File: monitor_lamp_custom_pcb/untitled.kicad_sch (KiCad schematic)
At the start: 9 parts, among them J2 VEML7700_Connection, J3 LD2410C_Connection, J4 Conn_01x02, Q2 IRLZ44N, U3 ESP32-C3_SUPERMINI_TH, U4 MAX40200AUK

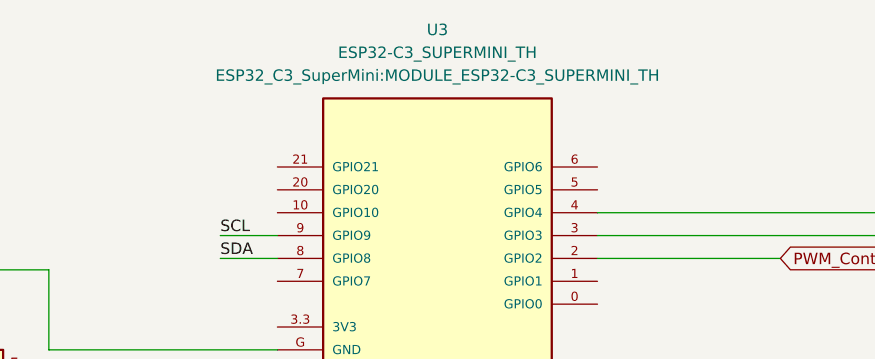
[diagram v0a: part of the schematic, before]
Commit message: Added custom library component to the project
In Kicad not all components are present in the default library, some sensors or modules have to be manually added importing symbols and footprint.
Putting this components inside the project is useful so if someone will download it, in is not necessary to search and import the components
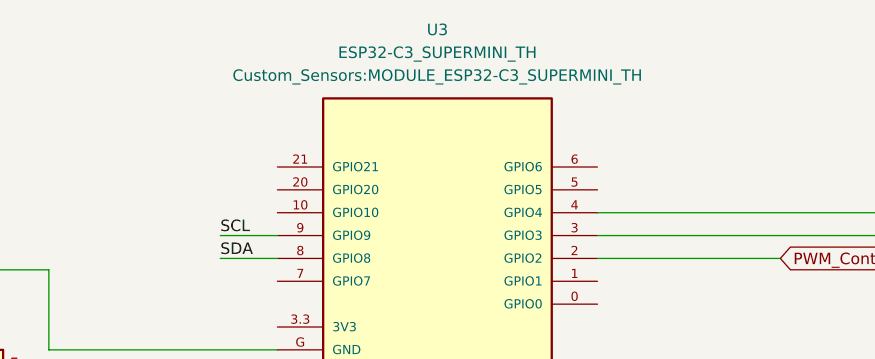
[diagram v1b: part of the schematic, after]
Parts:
- U3: footprint ESP32_C3_SuperMini:MODULE_ESP32-C3_SUPERMINI_TH -> Custom_Sensors:MODULE_ESP32-C3_SUPERMINI_TH

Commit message: Started to place component in the pcb design.
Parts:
- J4: footprint TerminalBlock_Phoenix:TerminalBlock_Phoenix_PT-1,5-2-5.0-H_1x02_P5.00mm_Horizontal -> TerminalBlock:TerminalBlock_Xinya_XY308-2.54-2P_1x02_P2.54mm_Horizontal
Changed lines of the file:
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@@
 			)
 		)
-		(property "Footprint" "TerminalBlock_Phoenix:TerminalBlock_Phoenix_PT-1,5-2-5.0-H_1x02_P5.00mm_Horizontal"
+		(property "Footprint" "TerminalBlock:TerminalBlock_Xinya_XY308-2.54-2P_1x02_P2.54mm_Horizontal"
 			(at 209.55 132.08 0)
 			(hide yes)

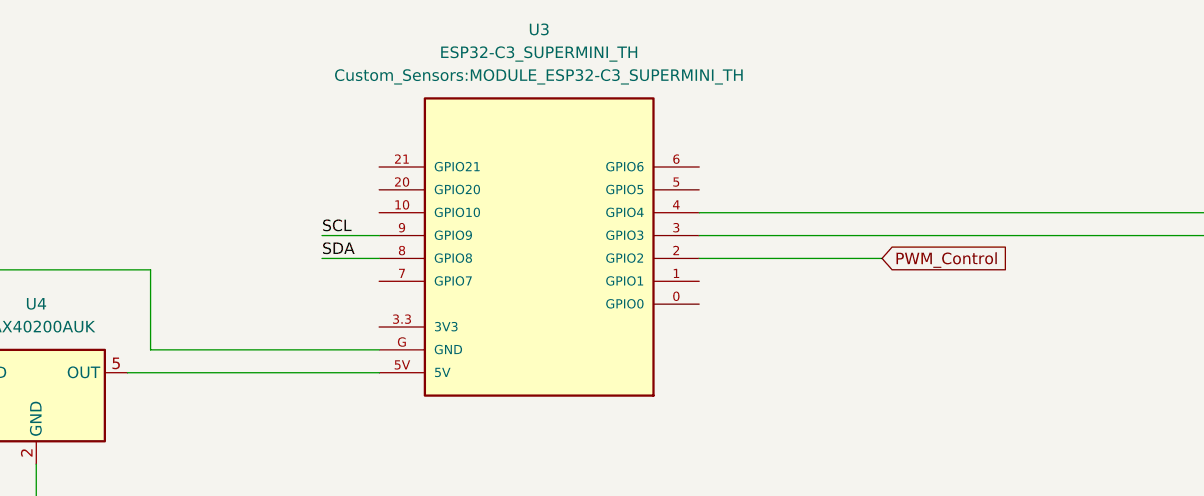
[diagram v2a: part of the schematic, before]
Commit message: Started to place components on the board layout
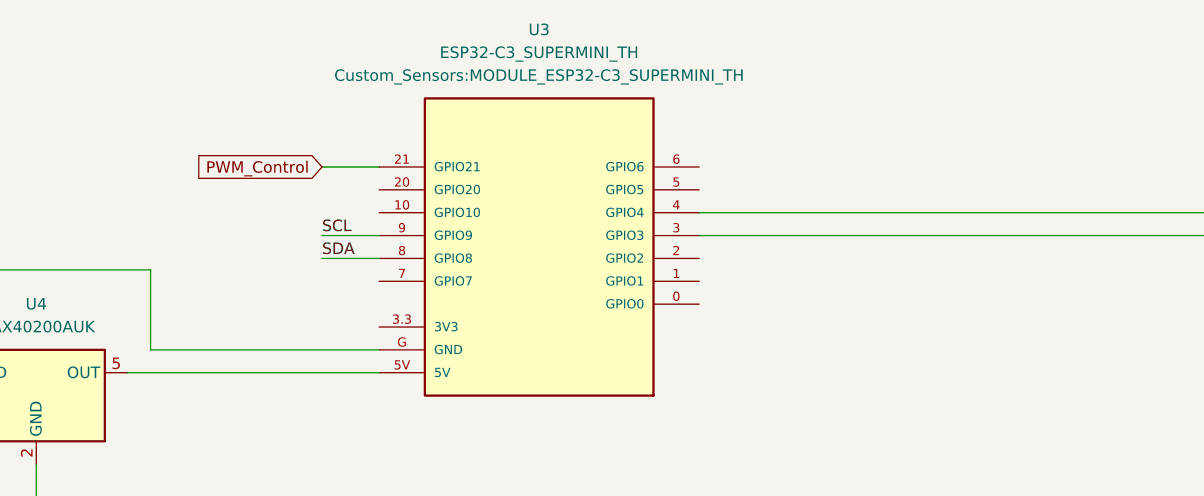
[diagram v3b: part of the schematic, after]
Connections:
- net PWM_Control: now also U3.21 (GPIO21); no longer U3.2 (GPIO2)
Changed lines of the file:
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@@
-	(wire
-		(pts
-			(xy 157.48 53.34) (xy 177.8 53.34)
-		)
-		(stroke
-			(width 0)
-			(type default)
-		)
-	)
 	(wire
 		(pts
@@
 		(pts
 			(xy 157.48 48.26) (xy 228.6 48.26)
+		)
+		(stroke
+			(width 0)
+			(type default)
+		)
+	)
+	(wire
+		(pts
+			(xy 115.57 43.18) (xy 121.92 43.18)
 		)
 		(stroke
@@
 	(global_label "PWM_Control"
 		(shape input)
-		(at 177.8 53.34 0)
+		(at 115.57 43.18 180)
 		(fields_autoplaced yes)
 		(effects
@@
 				(size 1.27 1.27)
 			)
-			(justify left)
+			(justify right)
 		)
 		(property "Intersheetrefs" "${INTERSHEET_REFS}"
-			(at 192.8197 53.34 0)
+			(at 100.5503 43.18 0)
 			(hide yes)
 			(show_name no)
@@
 					(size 1.27 1.27)
 				)
-				(justify left)
-			)
-		)
+				(justify right)
+			)
+		)

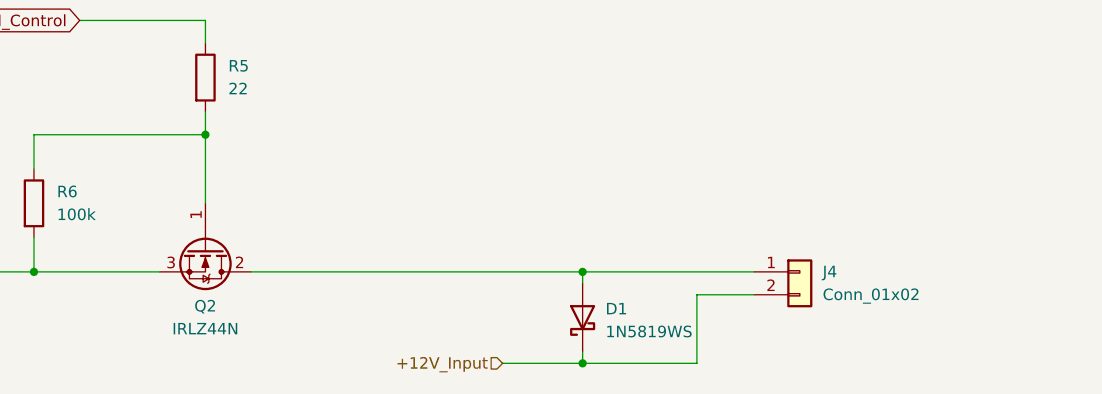
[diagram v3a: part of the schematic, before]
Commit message: Added almost all components to the board. Next step trace
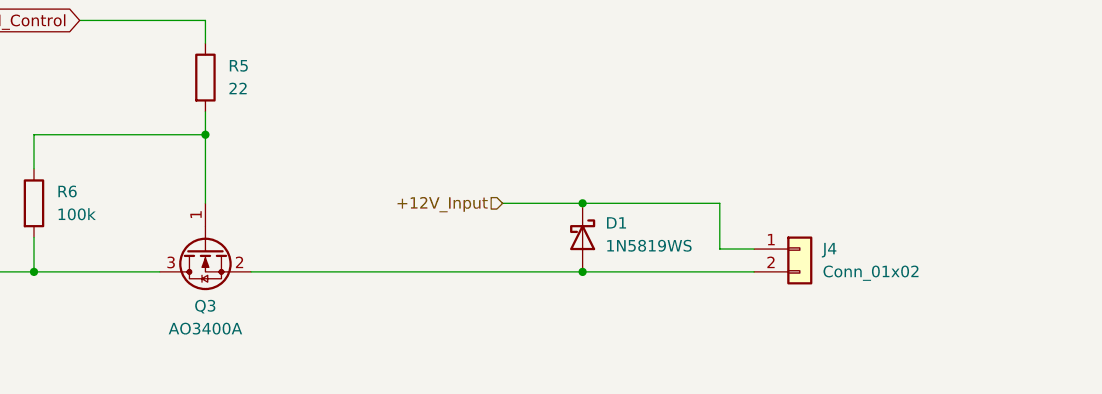
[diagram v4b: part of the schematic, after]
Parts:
- removed Q2: IRLZ44N, Package_TO_SOT_THT:TO-220-3_Vertical, symbol Transistor_FET:IRLZ44N
- added Q3: AO3400A, Package_TO_SOT_SMD:SOT-23, symbol Transistor_FET:AO3400A
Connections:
- net +12V_Input: now also J4.1 (Pin_1); no longer J4.2 (Pin_2)
- net GND: now also Q3.3 (D)
- net at R5.2, R6.1: now also Q3.1 (G)
- net at D1.2 (A): now also J4.2 (Pin_2), Q3.2 (S); no longer J4.1 (Pin_1)
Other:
- moved on the sheet: D1, J4
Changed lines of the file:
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@@
 	(paper "A4")
+	(junction
+		(at 185.42 132.08)
+		(diameter 0)
+		(color 0 0 0 0)
+	)
 	(junction
 		(at 124.46 132.08)
@@
 	)
 	(junction
-		(at 185.42 142.24)
-		(diameter 0)
-		(color 0 0 0 0)
-	)
-	(junction
-		(at 185.42 132.08)
+		(at 185.42 124.46)
 		(diameter 0)
 		(color 0 0 0 0)
@@
 	(wire
 		(pts
+			(xy 220.98 74.93) (xy 228.6 74.93)
+		)
+		(stroke
+			(width 0)
+			(type default)
+		)
+	)
+	(wire
+		(pts
+			(xy 93.98 66.04) (xy 121.92 66.04)
+		)
+		(stroke
+			(width 0)
+			(type default)
+		)
+	)
+	(wire
+		(pts
+			(xy 220.98 80.01) (xy 228.6 80.01)
+		)
+		(stroke
+			(width 0)
+			(type default)
+		)
+	)
+	(wire
+		(pts
+			(xy 176.53 124.46) (xy 185.42 124.46)
+		)
+		(stroke
+			(width 0)
+			(type default)
+		)
+	)
+	(wire
+		(pts
 			(xy 185.42 132.08) (xy 204.47 132.08)
 		)
@@
 	(wire
 		(pts
-			(xy 220.98 74.93) (xy 228.6 74.93)
-		)
-		(stroke
-			(width 0)
-			(type default)
-		)
-	)
-	(wire
-		(pts
-			(xy 93.98 66.04) (xy 121.92 66.04)
-		)
-		(stroke
-			(width 0)
-			(type default)
-		)
-	)
-	(wire
-		(pts
-			(xy 220.98 80.01) (xy 228.6 80.01)
-		)
-		(stroke
-			(width 0)
-			(type default)
-		)
-	)
-	(wire
-		(pts
-			(xy 185.42 140.97) (xy 185.42 142.24)
-		)
-		(stroke
-			(width 0)
-			(type default)
-		)
-	)
-	(wire
-		(pts
 			(xy 66.04 66.04) (xy 66.04 71.12)
 		)
@@
 	(wire
 		(pts
-			(xy 185.42 142.24) (xy 198.12 142.24)
-		)
-		(stroke
-			(width 0)
-			(type default)
-		)
-	)
-	(wire
-		(pts
 			(xy 96.52 54.61) (xy 96.52 63.5)
 		)
@@
 	(wire
 		(pts
-			(xy 185.42 132.08) (xy 185.42 133.35)
-		)
-		(stroke
-			(width 0)
-			(type default)
-		)
-	)
-	(wire
-		(pts
-			(xy 198.12 134.62) (xy 204.47 134.62)
+			(xy 204.47 129.54) (xy 200.66 129.54)
 		)
 		(stroke
@@
 	(wire
 		(pts
+			(xy 200.66 129.54) (xy 200.66 124.46)
+		)
+		(stroke
+			(width 0)
+			(type default)
+		)
+	)
+	(wire
+		(pts
+			(xy 200.66 124.46) (xy 185.42 124.46)
+		)
+		(stroke
+			(width 0)
+			(type default)
+		)
+	)
+	(wire
+		(pts
 			(xy 43.18 132.08) (xy 124.46 132.08)
-		)
-		(stroke
-			(width 0)
-			(type default)
-		)
-	)
-	(wire
-		(pts
-			(xy 198.12 142.24) (xy 198.12 134.62)
-		)
-		(stroke
-			(width 0)
-			(type default)
-		)
-	)
-	(wire
-		(pts
-			(xy 176.53 142.24) (xy 185.42 142.24)
 		)
 		(stroke
@@
 	(hierarchical_label "+12V_Input"
 		(shape input)
-		(at 176.53 142.24 180)
+		(at 176.53 124.46 180)
 		(effects
 			(font
@@
 	)
 	(symbol
-		(lib_id "Transistor_FET:IRLZ44N")
-		(at 143.51 129.54 270)
-		(unit 1)
-		(body_style 1)
-		(exclude_from_sim no)
-		(in_bom yes)
-		(on_board yes)
-		(in_pos_files yes)
-		(dnp no)
-		(fields_autoplaced yes)
-		(property "Reference" "Q2"
-			(at 143.51 135.89 90)
-			(show_name no)
-			(do_not_autoplace no)
-			(effects
-				(font
-					(size 1.27 1.27)
-				)
-			)
-		)
-		(property "Value" "IRLZ44N"
-			(at 143.51 138.43 90)
-			(show_name no)
-			(do_not_autoplace no)
-			(effects
-				(font
-					(size 1.27 1.27)
-				)
-			)
-		)
-		(property "Footprint" "Package_TO_SOT_THT:TO-220-3_Vertical"
-			(at 141.605 134.62 0)
-			(hide yes)
-			(show_name no)
-			(do_not_autoplace no)
-			(effects
-				(font
-					(size 1.27 1.27)
-					(italic yes)
-				)
-				(justify left)
-			)
-		)
-		(property "Datasheet" "http://www.irf.com/product-info/datasheets/data/irlz44n.pdf"
-			(at 139.7 134.62 0)
-			(hide yes)
-			(show_name no)
-			(do_not_autoplace no)
-			(effects
-				(font
-					(size 1.27 1.27)
-				)
-				(justify left)
-			)
-		)
-		(property "Description" "47A Id, 55V Vds, 22mOhm Rds Single N-Channel HEXFET Power MOSFET, TO-220AB"
-			(at 143.51 129.54 0)
-			(hide yes)
-			(show_name no)
-			(do_not_autoplace no)
-			(effects
-				(font
-					(size 1.27 1.27)
-				)
-			)
-		)
-		(pin "2"
-		)
-		(pin "1"
-		)
-		(pin "3"
-		)
-		(instances
-			(project "monitor_lamp_custom_pcb"
-				(path "/77ed2f8f-6c9e-49d8-b473-d071fcc9ba2f/0d662d48-a846-4d52-8851-1394daa2469c"
-					(reference "Q2")
-					(unit 1)
-				)
-			)
-		)
-	)
-	(symbol
 		(lib_id "power:GND")
 		(at 220.98 86.36 0)
@@
 	)
 	(symbol
+		(lib_id "Transistor_FET:AO3400A")
+		(at 143.51 129.54 90)
+		(mirror x)
+		(unit 1)
+		(body_style 1)
+		(exclude_from_sim no)
+		(in_bom yes)
+		(on_board yes)
+		(in_pos_files yes)
+		(dnp no)
+		(property "Reference" "Q3"
+			(at 143.51 135.89 90)
+			(show_name no)
+			(do_not_autoplace no)
+			(effects
+				(font
+					(size 1.27 1.27)
+				)
+			)
+		)
+		(property "Value" "AO3400A"
+			(at 143.51 138.43 90)
+			(show_name no)
+			(do_not_autoplace no)
+			(effects
+				(font
+					(size 1.27 1.27)
+				)
+			)
+		)
+		(property "Footprint" "Package_TO_SOT_SMD:SOT-23"
+			(at 145.415 134.62 0)
+			(hide yes)
+			(show_name no)
+			(do_not_autoplace no)
+			(effects
+				(font
+					(size 1.27 1.27)
+					(italic yes)
+				)
+				(justify left)
+			)
+		)
+		(property "Datasheet" "http://www.aosmd.com/pdfs/datasheet/AO3400A.pdf"
+			(at 147.32 134.62 0)
+			(hide yes)
+			(show_name no)
+			(do_not_autoplace no)
+			(effects
+				(font
+					(size 1.27 1.27)
+				)
+				(justify left)
+			)
+		)
+		(property "Description" "30V Vds, 5.7A Id, N-Channel MOSFET, SOT-23"
+			(at 143.51 129.54 0)
+			(hide yes)
+			(show_name no)
+			(do_not_autoplace no)
+			(effects
+				(font
+					(size 1.27 1.27)
+				)
+			)
+		)
+		(pin "3"
+		)
+		(pin "2"
+		)
+		(pin "1"
+		)
+		(instances
+			(project "monitor_lamp_custom_pcb"
+				(path "/77ed2f8f-6c9e-49d8-b473-d071fcc9ba2f/0d662d48-a846-4d52-8851-1394daa2469c"
+					(reference "Q3")
+					(unit 1)
+				)
+			)
+		)
+	)
+	(symbol
 		(lib_id "Connector_Generic:Conn_01x02")
-		(at 209.55 132.08 0)
+		(at 209.55 129.54 0)
 		(unit 1)
 		(body_style 1)
@@
 		(fields_autoplaced yes)
 		(property "Reference" "J4"
+			(at 212.09 129.5399 0)
+			(show_name no)
+			(do_not_autoplace no)
+			(effects
+				(font
+					(size 1.27 1.27)
+				)
+				(justify left)
+			)
+		)
+		(property "Value" "Conn_01x02"
 			(at 212.09 132.0799 0)
 			(show_name no)
@@
 			)
 		)
-		(property "Value" "Conn_01x02"
-			(at 212.09 134.6199 0)
-			(show_name no)
-			(do_not_autoplace no)
-			(effects
-				(font
-					(size 1.27 1.27)
-				)
-				(justify left)
-			)
-		)
 		(property "Footprint" "TerminalBlock:TerminalBlock_Xinya_XY308-2.54-2P_1x02_P2.54mm_Horizontal"
-			(at 209.55 132.08 0)
+			(at 209.55 129.54 0)
 			(hide yes)
 			(show_name no)
@@
 		)
 		(property "Datasheet" ""
-			(at 209.55 132.08 0)
+			(at 209.55 129.54 0)
 			(hide yes)
 			(show_name no)
@@
 		)
 		(property "Description" "Generic connector, single row, 01x02, script generated (kicad-library-utils/schlib/autogen/connector/)"
-			(at 209.55 132.08 0)
+			(at 209.55 129.54 0)
 			(hide yes)
 			(show_name no)
@@
 	(symbol
 		(lib_id "Diode:1N5819WS")
-		(at 185.42 137.16 90)
+		(at 185.42 128.27 270)
 		(unit 1)
 		(body_style 1)
@@
 		(fields_autoplaced yes)
 		(property "Reference" "D1"
-			(at 187.96 136.2074 90)
-			(show_name no)
-			(do_not_autoplace no)
-			(effects
-				(font
-					(size 1.27 1.27)
-				)
-				(justify right)
+			(at 187.96 126.6824 90)
+			(show_name no)
+			(do_not_autoplace no)
+			(effects
+				(font
+					(size 1.27 1.27)
+				)
+				(justify left)
 			)
 		)
 		(property "Value" "1N5819WS"
-			(at 187.96 138.7474 90)
-			(show_name no)
-			(do_not_autoplace no)
-			(effects
-				(font
-					(size 1.27 1.27)
-				)
-				(justify right)
+			(at 187.96 129.2224 90)
+			(show_name no)
+			(do_not_autoplace no)
+			(effects
+				(font
+					(size 1.27 1.27)
+				)
+				(justify left)
 			)
 		)
 		(property "Footprint" "Diode_SMD:D_SOD-323"
-			(at 189.865 137.16 0)
+			(at 180.975 128.27 0)
 			(hide yes)
 			(show_name no)
@@
 		)
 		(property "Datasheet" "https://datasheet.lcsc.com/lcsc/2204281430_Guangdong-Hottech-1N5819WS_C191023.pdf"
-			(at 185.42 137.16 0)
+			(at 185.42 128.27 0)
 			(hide yes)
 			(show_name no)
@@
 		)
 		(property "Description" "40V 600mV@1A 1A SOD-323 Schottky Barrier Diodes, SOD-323"
-			(at 185.42 137.16 0)
-			(hide yes)
-			(show_name no)
+			(at 185.42 128.27 0)
+			(hide yes)
+			(show_name no)

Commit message: Placed all components, changed the J2 & J3 connectors
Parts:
- J2, J3: footprint Connector_PinHeader_2.54mm:PinHeader_1x04_P2.54mm_Horizontal -> Connector_JST:JST_SH_BM04B-SRSS-TB_1x04-1MP_P1.00mm_Vertical
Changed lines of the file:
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@@
 			)
 		)
-		(property "Footprint" "Connector_PinHeader_2.54mm:PinHeader_1x04_P2.54mm_Horizontal"
+		(property "Footprint" "Connector_JST:JST_SH_BM04B-SRSS-TB_1x04-1MP_P1.00mm_Vertical"
 			(at 233.68 77.47 0)
 			(hide yes)
@@
 			)
 		)
-		(property "Footprint" "Connector_PinHeader_2.54mm:PinHeader_1x04_P2.54mm_Horizontal"
+		(property "Footprint" "Connector_JST:JST_SH_BM04B-SRSS-TB_1x04-1MP_P1.00mm_Vertical"
 			(at 233.68 48.26 0)
 			(hide yes)

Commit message: Tracing some routes
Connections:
- net +5V is gone; now on net 5V_Protected: J2.1 (Pin_1), J3.1 (Pin_1)
- net 5V_Protected: now reaches U3.5V, U4.5 (OUT)
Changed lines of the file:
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@@
 	(wire
 		(pts
-			(xy 220.98 45.72) (xy 228.6 45.72)
+			(xy 215.9 45.72) (xy 228.6 45.72)
 		)
 		(stroke
@@
 	(wire
 		(pts
-			(xy 220.98 74.93) (xy 228.6 74.93)
+			(xy 215.9 74.93) (xy 228.6 74.93)
 		)
 		(stroke
@@
 		)
 	)
-	(label "+5V"
-		(at 220.98 74.93 0)
-		(effects
-			(font
-				(size 1.27 1.27)
-			)
-			(justify left bottom)
-		)
-	)
-	(label "+5V"
-		(at 220.98 45.72 0)
-		(effects
-			(font
+	(label "5V_Protected"
+		(at 97.79 66.04 0)
+		(effects
+			(font
+				(size 1.27 1.27)
+			)
+			(justify left bottom)
+		)
+	)
+	(label "5V_Protected"
+		(at 215.9 74.93 0)
+		(effects
+			(font
+				(size 1.27 1.27)
+			)
+			(justify left bottom)
+		)
+	)
+	(label "5V_Protected"
+		(at 215.9 45.72 0)
+		(effects
+			(font

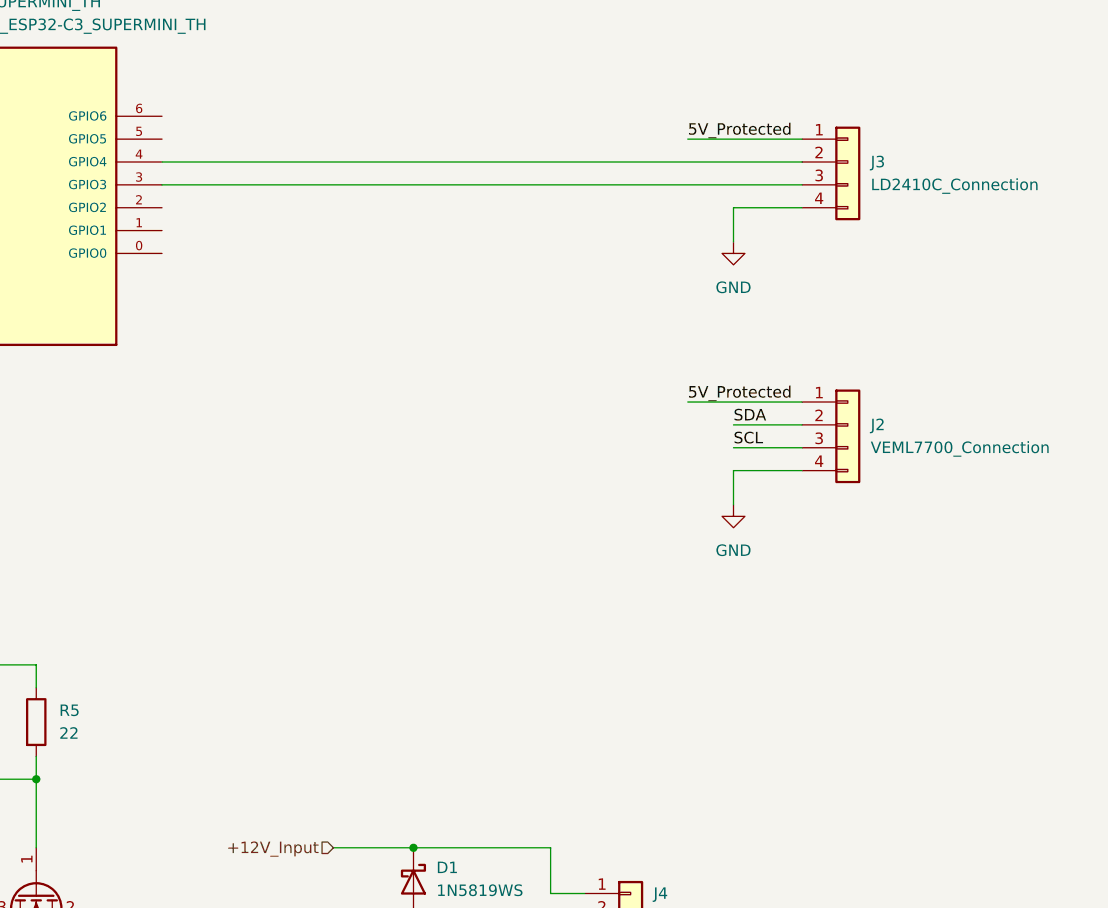
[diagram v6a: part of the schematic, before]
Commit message: Added connection for temp sensor
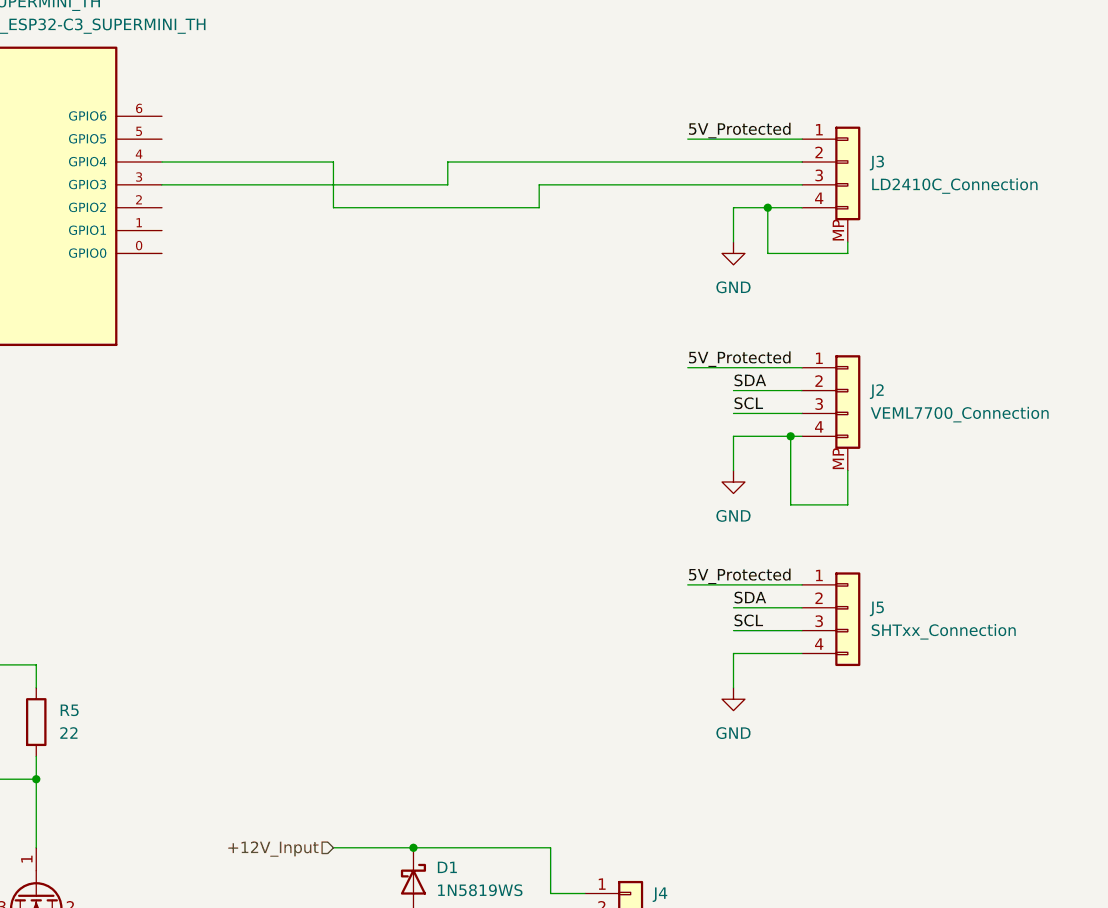
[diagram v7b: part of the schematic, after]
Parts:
- added J5: SHTxx_Connection, Connector_PinHeader_2.54mm:PinHeader_1x04_P2.54mm_Vertical, symbol Connector_Generic:Conn_01x04
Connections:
- net 5V_Protected: now also J5.1 (Pin_1)
- net GND: now also J2.MP, J3.MP, J5.4 (Pin_4)
- net SCL: now also J5.3 (Pin_3)
- net SDA: now also J5.2 (Pin_2)
- net at J3.2 (Pin_2): now also U3.3 (GPIO3); no longer U3.4 (GPIO4)
- net at J3.3 (Pin_3): now also U3.4 (GPIO4); no longer U3.3 (GPIO3)
